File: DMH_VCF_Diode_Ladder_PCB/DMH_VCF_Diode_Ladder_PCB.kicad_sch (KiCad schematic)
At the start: 0 parts

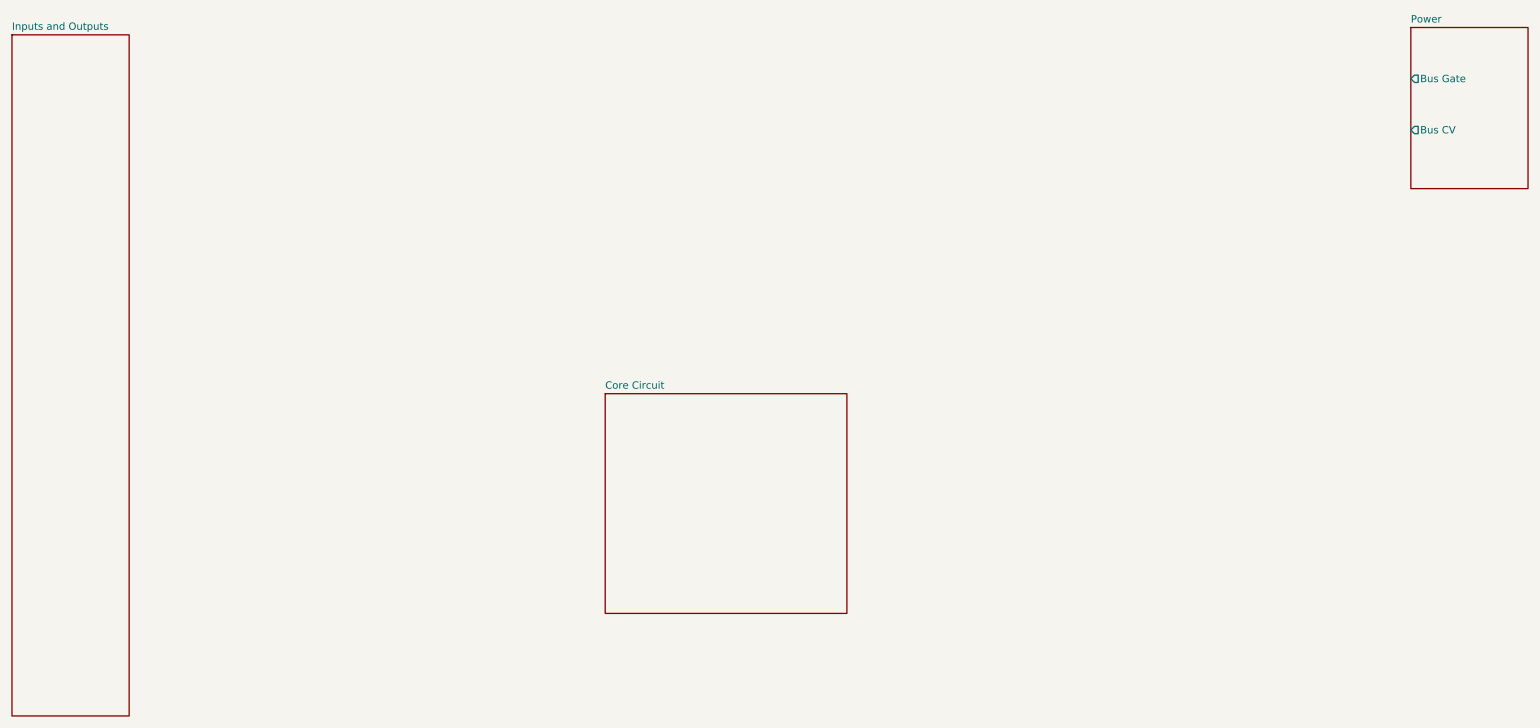
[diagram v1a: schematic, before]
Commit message: Finished schematic and added Bus CV 2 pot
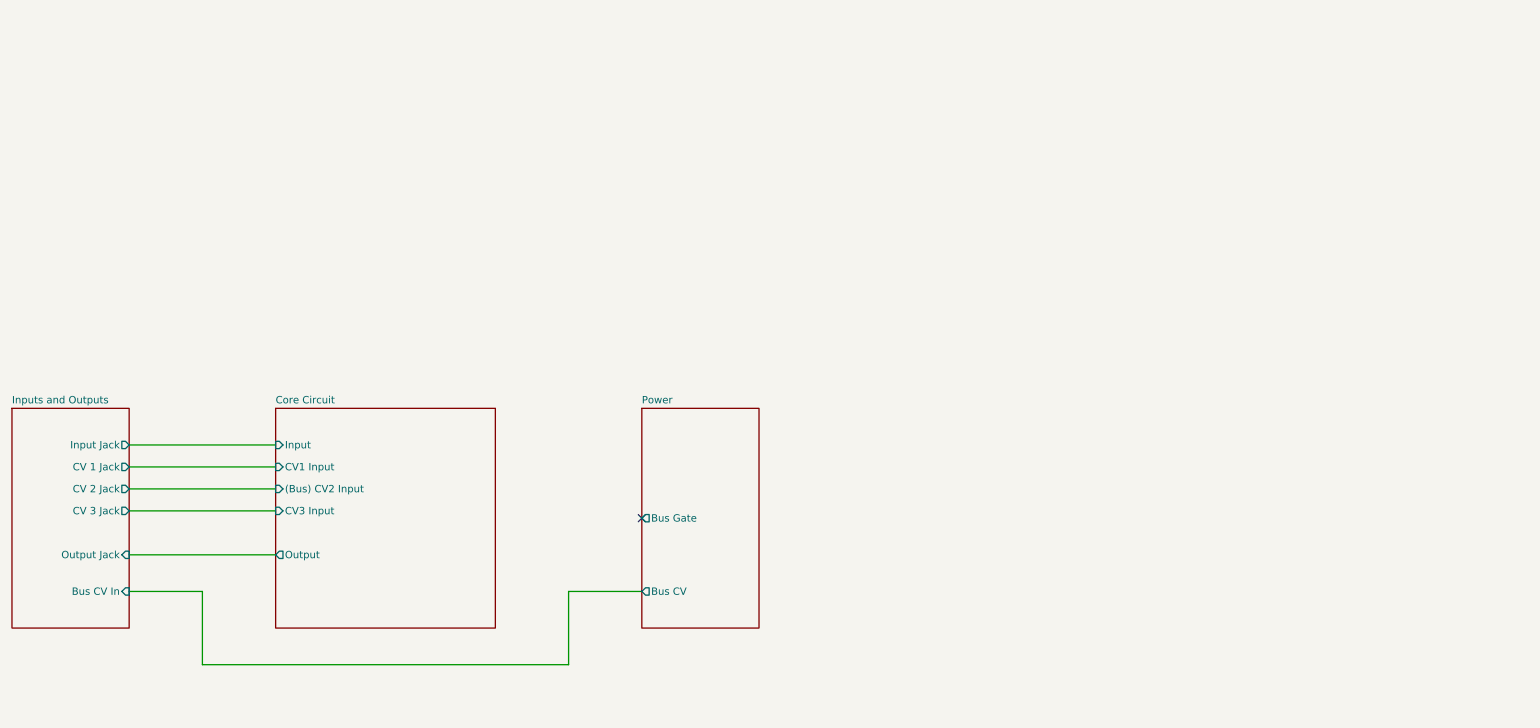
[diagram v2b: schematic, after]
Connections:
- no-connect marks 0 -> 1
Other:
- sheet Core Circuit ports: added (Bus) CV2 Input, CV1 Input, CV3 Input, Input, Output; removed none
- sheet Inputs and Outputs ports: added Bus CV In, CV 1 Jack, CV 2 Jack, CV 3 Jack, Input Jack, Output Jack; removed none
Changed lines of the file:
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@@
 		(comment 1 "PCB for 10cm Kosmo format synthesizer module")
 	)
+	(no_connect
+		(at 127 101.6)
+	)
+	(wire
+		(pts
+			(xy 114.3 114.3) (xy 127 114.3)
+		)
+		(stroke
+			(width 0)
+			(type default)
+		)
+	)
+	(wire
+		(pts
+			(xy 38.1 88.9) (xy 63.5 88.9)
+		)
+		(stroke
+			(width 0)
+			(type default)
+		)
+	)
+	(wire
+		(pts
+			(xy 38.1 96.52) (xy 63.5 96.52)
+		)
+		(stroke
+			(width 0)
+			(type default)
+		)
+	)
+	(wire
+		(pts
+			(xy 50.8 127) (xy 114.3 127)
+		)
+		(stroke
+			(width 0)
+			(type default)
+		)
+	)
+	(wire
+		(pts
+			(xy 114.3 127) (xy 114.3 114.3)
+		)
+		(stroke
+			(width 0)
+			(type default)
+		)
+	)
+	(wire
+		(pts
+			(xy 38.1 92.71) (xy 63.5 92.71)
+		)
+		(stroke
+			(width 0)
+			(type default)
+		)
+	)
+	(wire
+		(pts
+			(xy 38.1 107.95) (xy 63.5 107.95)
+		)
+		(stroke
+			(width 0)
+			(type default)
+		)
+	)
+	(wire
+		(pts
+			(xy 50.8 114.3) (xy 50.8 127)
+		)
+		(stroke
+			(width 0)
+			(type default)
+		)
+	)
+	(wire
+		(pts
+			(xy 38.1 100.33) (xy 63.5 100.33)
+		)
+		(stroke
+			(width 0)
+			(type default)
+		)
+	)
+	(wire
+		(pts
+			(xy 38.1 114.3) (xy 50.8 114.3)
+		)
+		(stroke
+			(width 0)
+			(type default)
+		)
+	)
 	(sheet
-		(at 260.35 16.51)
-		(size 20.32 27.94)
+		(at 127 82.55)
+		(size 20.32 38.1)
 		(fields_autoplaced yes)
 		(stroke
@@
 		)
 		(property "Sheetname" "Power"
-			(at 260.35 15.7984 0)
+			(at 127 81.8384 0)
 			(effects
 				(font
@@
 		)
 		(property "Sheetfile" "Power.kicad_sch"
-			(at 260.35 45.0346 0)
+			(at 127 121.2346 0)
 			(effects
 				(font
@@
 		)
 		(pin "Bus Gate" output
-			(at 260.35 25.4 180)
+			(at 127 101.6 180)
 			(effects
 				(font
@@
 		)
 		(pin "Bus CV" output
-			(at 260.35 34.29 180)
+			(at 127 114.3 180)
 			(effects
 				(font
@@
 	)
 	(sheet
-		(at 120.65 80.01)
-		(size 41.91 38.1)
+		(at 63.5 82.55)
+		(size 38.1 38.1)
 		(fields_autoplaced yes)
 		(stroke
@@
 		)
 		(property "Sheetname" "Core Circuit"
-			(at 120.65 79.2984 0)
+			(at 63.5 81.8384 0)
 			(effects
 				(font
@@
 		)
 		(property "Sheetfile" "Core_Circuit.kicad_sch"
-			(at 120.65 118.6946 0)
+			(at 63.5 121.2346 0)
 			(effects
 				(font
@@
 				(justify left top)
 				(hide yes)
+			)
+		)
+		(pin "Output" output
+			(at 63.5 107.95 180)
+			(effects
+				(font
+					(size 1.27 1.27)
+				)
+				(justify left)
+			)
+		)
+		(pin "(Bus) CV2 Input" input
+			(at 63.5 96.52 180)
+			(effects
+				(font
+					(size 1.27 1.27)
+				)
+				(justify left)
+			)
+		)
+		(pin "CV3 Input" input
+			(at 63.5 100.33 180)
+			(effects
+				(font
+					(size 1.27 1.27)
+				)
+				(justify left)
+			)
+		)
+		(pin "Input" input
+			(at 63.5 88.9 180)
+			(effects
+				(font
+					(size 1.27 1.27)
+				)
+				(justify left)
+			)
+		)
+		(pin "CV1 Input" input
+			(at 63.5 92.71 180)
+			(effects
+				(font
+					(size 1.27 1.27)
+				)
+				(justify left)
 			)
 		)
@@
 	)
 	(sheet
-		(at 17.78 17.78)
-		(size 20.32 118.11)
+		(at 17.78 82.55)
+		(size 20.32 38.1)
 		(fields_autoplaced yes)
 		(stroke
@@
 		)
 		(property "Sheetname" "Inputs and Outputs"
-			(at 17.78 17.0684 0)
+			(at 17.78 81.8384 0)
 			(effects
 				(font
@@
 		)
 		(property "Sheetfile" "Inputs_and_Outputs.kicad_sch"
-			(at 17.78 136.4746 0)
+			(at 17.78 121.2346 0)
 			(effects
 				(font
@@
 			)
 		)
+		(pin "Output Jack" input
+			(at 38.1 107.95 0)
+			(effects
+				(font
+					(size 1.27 1.27)
+				)
+				(justify right)
+			)
+		)
+		(pin "Input Jack" output
+			(at 38.1 88.9 0)
+			(effects
+				(font
+					(size 1.27 1.27)
+				)
+				(justify right)
+			)
+		)
+		(pin "CV 1 Jack" output
+			(at 38.1 92.71 0)
+			(effects
+				(font
+					(size 1.27 1.27)
+				)
+				(justify right)
+			)
+		)
+		(pin "CV 2 Jack" output
+			(at 38.1 96.52 0)
+			(effects
+				(font
+					(size 1.27 1.27)
+				)
+				(justify right)
+			)
+		)
+		(pin "CV 3 Jack" output
+			(at 38.1 100.33 0)
+			(effects
+				(font
+					(size 1.27 1.27)
+				)
+				(justify right)
+			)
+		)
+		(pin "Bus CV In" input
+			(at 38.1 114.3 0)
+			(effects
+				(font
+					(size 1.27 1.27)
+				)
+				(justify right)
+			)
+		)
